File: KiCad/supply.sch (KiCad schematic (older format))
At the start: 59 parts, among them IC12 74HC00PW, IC13 SN74LVC1G126DCKR, IC4 TPS7A0518PDBVT, T3 BSS138APW, U1 LM62440-Q1, U2 LM62440-Q1

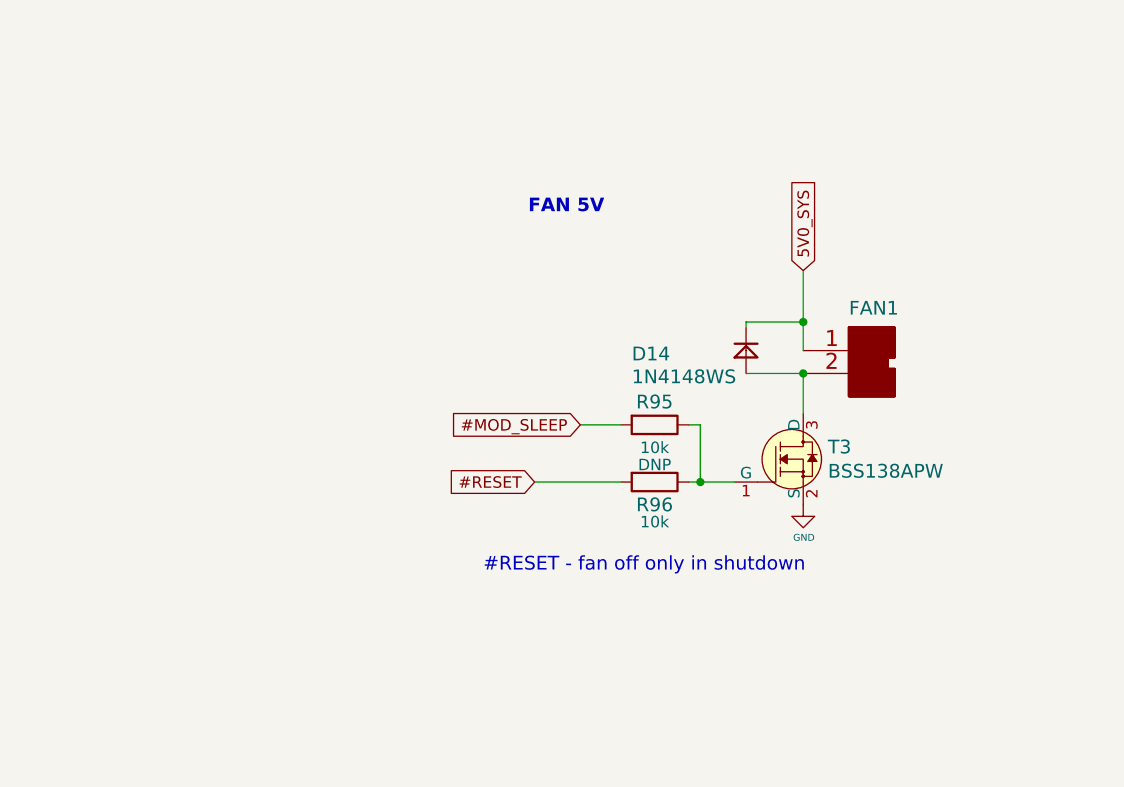
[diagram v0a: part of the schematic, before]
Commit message: Change fan design to match Nvidia. Change user button and led pins
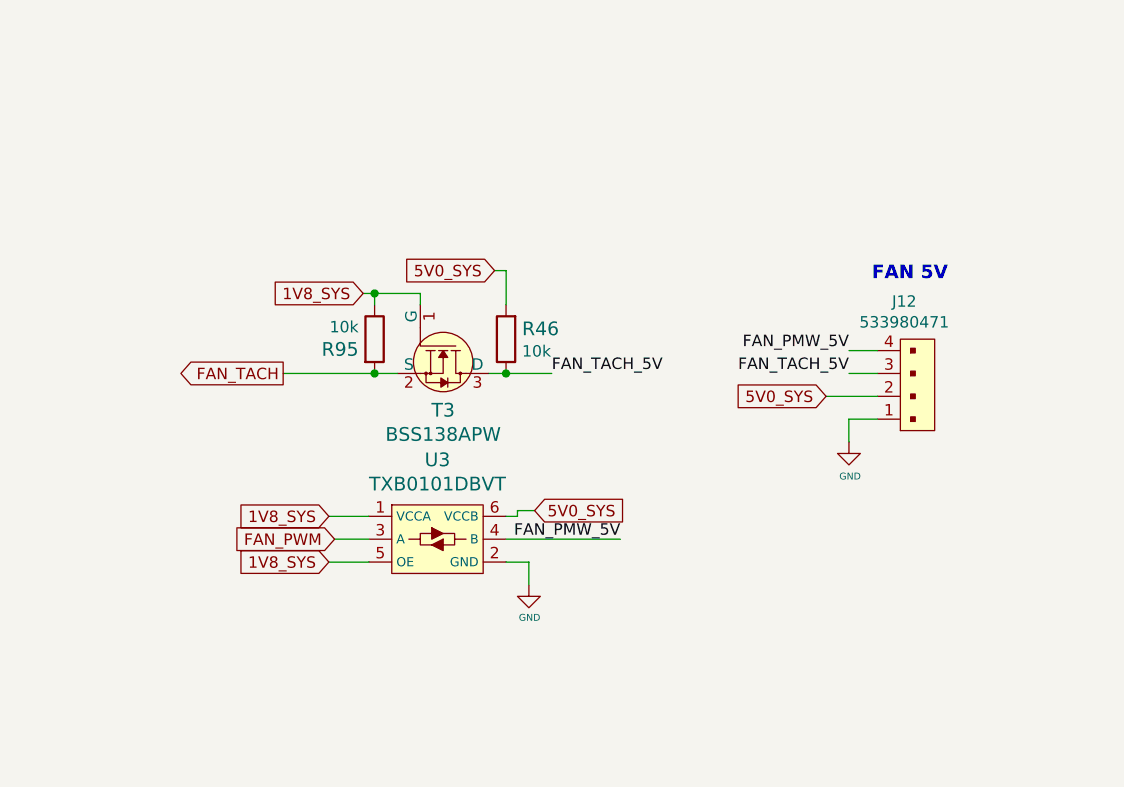
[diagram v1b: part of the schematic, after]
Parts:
- removed D14: 1N4148WS, jetson-nano-baseboard-footprints:SOD-323, symbol jetson-nano-baseboard:diode
- removed FAN1: ~, jetson-nano-baseboard-footprints:molex_2223-2021, symbol jetson-nano-baseboard:molex_2223-2021
- removed R96: R_10k_0402, jetson-nano-baseboard-footprints:0402-res, symbol jetson-nano-baseboard:R_10k_0402
- added J12: 533980471, jetson-nano-baseboard-footprints:Molex_PicoBlade_53398-0471_1x04-1MP_P1.25mm_Vertical, symbol jetson-nano-baseboard:533980471
- added R46: R_10k_0402, jetson-nano-baseboard-footprints:0402-res, symbol jetson-nano-baseboard:R_10k_0402
- added U3: TXB0101DBVT, jetson-nano-baseboard-footprints:SOT-23-6, symbol jetson-nano-baseboard:TXB0101DBVT
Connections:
- net 1V8_SYS: now also R95.1, T3.1 (G), U3.1 (VCCA), U3.5 (OE)
- net 5V0_SYS: now also J12.2, R46.2, U3.6 (VCCB)
- net GND: now also J12.1, U3.2 (GND); no longer T3.2 (S)
- net FAN_TACH_5V: now reaches T3.3 (D)
- net FAN_TACH_5V: now also J12.3, R46.1
- net #MOD_SLEEP renamed FAN_TACH
- net FAN_TACH: now also T3.2 (S)
- new net FAN_PMW_5V: J12.4, U3.4 (B)
- new net FAN_PWM: U3.3 (A)
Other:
- note removed: "#RESET - fan off only in shutdown"
- moved on the sheet: R95, T3
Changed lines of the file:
@@
 Text Notes 8075 4750 0    59   ~ 12
 Power sequencer
-Text Notes 9897 8682 0    59   ~ 12
-FAN 5V
 Wire Wire Line
 	12870 7550 12970 7550
 Wire Wire Line
 	12870 7650 12870 7550
-Text Notes 9700 10250 0    60   ~ 0
-#RESET - fan off only in shutdown
 Text Notes 9500 6575 0    60   ~ 0
 #PWR_RST
@@
 Text GLabel 13944 2408 1    50   Input ~ 0
 VIN
-Text GLabel 11100 8925 1    50   Input ~ 0
-5V0_SYS
 Text GLabel 9975 5000 1    50   Input ~ 0
 5V0_SYS
@@
 $EndComp
 $Comp
-L jetson-nano-baseboard:GND #GND_079
-U 1 1 5E7103C3
-P 11100 9950
-F 0 "#GND_079" H 11100 9950 20  0001 C CNN
-F 1 "GND" H 11103 9807 30  0000 C CNN
-F 2 "" H 11100 9950 70  0001 C CNN
-F 3 "" H 11100 9950 70  0001 C CNN
-	1    11100 9950
-	1    0    0    -1
-$EndComp
-$Comp
 L jetson-nano-baseboard:GND #GND_080
 U 1 1 5E7103C1
@@
 $EndComp
 $Comp
-L jetson-nano-baseboard:molex_2223-2021 FAN1
-U 1 1 5E7103AC
-P 11100 9275
-F 0 "FAN1" H 11300 9425 60  0000 L BNN
-F 1 "~" H 11100 9275 50  0001 C CNN
-F 2 "jetson-nano-baseboard-footprints:molex_2223-2021" H 11100 9275 50  0001 C CNN
-F 3 "" H 11100 9275 50  0001 C CNN
-F 4 "2223-2021" H 43  -12311 50  0001 C CNN "MPN"
-F 5 "Molex" H 43  -12311 50  0001 C CNN "Manufacturer"
-	1    11100 9275
-	1    0    0    -1
-$EndComp
-$Comp
-L jetson-nano-baseboard:diode D14
-U 1 1 5E7103AB
-P 10850 9275
-F 0 "D14" H 10350 9225 60  0000 L BNN
-F 1 "1N4148WS" H 10350 9125 60  0000 L BNN
-F 2 "jetson-nano-baseboard-footprints:SOD-323" H 10350 9125 60  0001 C CNN
-F 3 "" H 10350 9125 60  0001 C CNN
-F 4 "1N4148WS" H -7  -12311 50  0001 C CNN "MPN"
-F 5 "ON Semiconductor" H -7  -12311 50  0001 C CNN "Manufacturer"
-	1    10850 9275
-	1    0    0    -1
-$EndComp
-$Comp
 L jetson-nano-baseboard:Testpad TP42
 U 1 1 5E7103A8
@@
 	13875 6250 14075 6250
 Connection ~ 14075 6250
-Wire Wire Line
-	10800 9850 10650 9850
-Wire Wire Line
-	10850 9375 11100 9375
-Wire Wire Line
-	11100 9375 11100 9550
-Connection ~ 11100 9375
-Wire Wire Line
-	11100 8925 11100 9150
-Wire Wire Line
-	10850 9175 10850 9150
-Wire Wire Line
-	10850 9150 11100 9150
-Connection ~ 11100 9150
-Wire Wire Line
-	11100 9150 11100 9275
-$Comp
-L jetson-nano-baseboard:BSS138APW T3
-U 1 1 607CDC49
-P 11100 9750
-F 0 "T3" H 11208 9803 60  0000 L CNN
-F 1 "BSS138APW" H 11208 9697 60  0000 L CNN
-F 2 "jetson-nano-baseboard-footprints:SC70-3" H 11300 9950 60  0001 L CNN
-F 3 "" H 11300 10050 60  0001 L CNN
-F 4 "BSS138PW" H 11300 10250 60  0001 L CNN "MPN"
-F 5 "ON Semiconductor" H 11300 10850 60  0001 L CNN "Manufacturer"
-	1    11100 9750
-	1    0    0    -1
-$EndComp
 Text GLabel 14525 6250 2    50   Input ~ 0
 PWR_EN
-Text GLabel 9925 9850 0    50   Input ~ 0
-#RESET
 Text GLabel 9475 6450 0    50   Input ~ 0
 #SHUTDOWN_REQ
@@
 	0    1    1    0
 $EndComp
-Text GLabel 10125 9600 0    50   Input ~ 0
-#MOD_SLEEP
 Text GLabel 12225 5425 0    50   Input ~ 0
 PWR_GOOD
@@
 Wire Wire Line
 	10675 5750 10675 5000
-$Comp
-L jetson-nano-baseboard:R_10k_0402 R95
-U 1 1 6202E2C7
-P 10450 9600
-F 0 "R95" H 10450 9500 60  0000 C CNN
-F 1 "R_10k_0402" H 10450 9450 60  0001 C CNN
-F 2 "jetson-nano-baseboard-footprints:0402-res" H 10650 9800 60  0001 L CNN
-F 3 "" H 10450 9600 50  0001 C CNN
-F 4 "VISHAY" H 10650 10000 60  0001 L CNN "Manufacturer"
-F 5 "CRCW040210K0FKEDHP" H 10650 9900 60  0001 L CNN "MPN"
-F 6 "10k" H 10450 9700 50  0000 C CNN "Val"
-	1    10450 9600
-	-1   0    0    1
-$EndComp
-Wire Wire Line
-	10600 9600 10650 9600
-Wire Wire Line
-	10650 9600 10650 9850
-Wire Wire Line
-	10650 9850 10600 9850
-Connection ~ 10650 9850
-Wire Wire Line
-	9925 9850 10300 9850
-Wire Wire Line
-	10125 9600 10300 9600
 $Comp
 L jetson-nano-baseboard:R_200k_0402 R84
@@
 Wire Wire Line
 	13350 5625 13450 5625
-$Comp
-L jetson-nano-baseboard:R_10k_0402 R96
-U 1 1 6202F8EF
-P 10450 9850
-F 0 "R96" H 10450 9950 60  0000 C CNN
-F 1 "R_10k_0402" H 10450 9700 60  0001 C CNN
-F 2 "jetson-nano-baseboard-footprints:0402-res" H 10650 10050 60  0001 L CNN
-F 3 "" H 10450 9850 50  0001 C CNN
-F 4 "VISHAY" H 10650 10250 60  0001 L CNN "Manufacturer"
-F 5 "CRCW040210K0FKEDHP" H 10650 10150 60  0001 L CNN "MPN"
-F 6 "10k" H 10450 10025 50  0000 C CNN "Val"
-F 7 "DNP" H 10450 9775 50  0000 C CNN "DNP"
-	1    10450 9850
-	-1   0    0    1
-$EndComp
 $Comp
 L jetson-nano-baseboard:Testpad TP40
@@
 Wire Wire Line
 	1425 5250 2700 5250
+Text GLabel 9050 10100 0    50   Input ~ 0
+FAN_PWM
+Text GLabel 9025 10000 0    50   Input ~ 0
+1V8_SYS
+Wire Wire Line
+	9025 10000 9200 10000
+Wire Wire Line
+	9050 10100 9200 10100
+Text GLabel 9025 10200 0    50   Input ~ 0
+1V8_SYS
+Wire Wire Line
+	9025 10200 9200 10200
+Wire Wire Line
+	9800 10100 10300 10100
+Text Label 10300 10100 2    50   ~ 0
+FAN_PMW_5V
+Text GLabel 9925 9975 2    50   Input ~ 0
+5V0_SYS
+Wire Wire Line
+	9925 9975 9850 9975
+Wire Wire Line
+	9850 9975 9850 10000
+Wire Wire Line
+	9850 10000 9800 10000
+Wire Wire Line
+	9800 10200 9900 10200
+Wire Wire Line
+	9900 10200 9900 10300
+$Comp
+L jetson-nano-baseboard:GND #GND_0151
+U 1 1 61D0F309
+P 9900 10300
+F 0 "#GND_0151" H 9900 10300 20  0001 C CNN
+F 1 "GND" H 9903 10157 30  0000 C CNN
+F 2 "" H 9900 10300 70  0001 C CNN
+F 3 "" H 9900 10300 70  0001 C CNN
+	1    9900 10300
+	1    0    0    -1
+$EndComp
+$Comp
+L jetson-nano-baseboard:TXB0101DBVT U3
+U 1 1 62015C4C
+P 9500 10100
+F 0 "U3" H 9500 10447 60  0000 C CNN
+F 1 "TXB0101DBVT" H 9500 10341 60  0000 C CNN
+F 2 "jetson-nano-baseboard-footprints:SOT-23-6" H 9700 10300 60  0001 L CNN
+F 3 "https://www.ti.com/general/docs/suppproductinfo.tsp?distId=10&gotoUrl=https%3A%2F%2Fwww.ti.com%2Flit%2Fgpn%2Ftxb0101" H 9700 10400 60  0001 L CNN
+F 4 "TXB0101DBVT" H 9700 10500 60  0001 L CNN "MPN"
+F 5 "Texas Instruments" H 9700 10600 60  0001 L CNN "Manufacturer"
+	1    9500 10100
+	1    0    0    -1
+$EndComp
+Text Notes 11400 8975 0    59   ~ 12
+FAN 5V
+Text Label 11300 9375 2    50   ~ 0
+FAN_TACH_5V
+Wire Wire Line
+	11425 9375 11300 9375
+Text Label 11300 9275 2    50   ~ 0
+FAN_PMW_5V
+Wire Wire Line
+	11425 9275 11300 9275
+Text GLabel 11200 9475 0    50   Input ~ 0
+5V0_SYS
+Wire Wire Line
+	11200 9475 11425 9475
+Wire Wire Line
+	11425 9575 11300 9575
+Wire Wire Line
+	11300 9575 11300 9675
+$Comp
+L jetson-nano-baseboard:GND #GND_0157
+U 1 1 61E9E5AC
+P 11300 9675
+F 0 "#GND_0157" H 11300 9675 20  0001 C CNN
+F 1 "GND" H 11305 9525 30  0000 C CNN
+F 2 "" H 11300 9675 70  0001 C CNN
+F 3 "" H 11300 9675 70  0001 C CNN
+	1    11300 9675
+	1    0    0    -1
+$EndComp
+$Comp
+L jetson-nano-baseboard:533980471 J12
+U 1 1 6210B794
+P 11625 9425
+F 0 "J12" H 11542 9060 50  0000 C CNN
+F 1 "533980471" H 11542 9151 50  0000 C CNN
+F 2 "jetson-nano-baseboard-footprints:Molex_PicoBlade_53398-0471_1x04-1MP_P1.25mm_Vertical" H 11725 9325 50  0001 L BNN
+F 3 "https://www.molex.com/molex/products/part-detail/pcb_headers/0533980471" H 11525 9225 50  0001 L BNN
+F 4 "Molex" H 11725 9475 50  0001 L BNN "Manufacturer"
+F 5 "0533980471" H 11975 9425 50  0001 C CNN "MPN"
+	1    11625 9425
+	1    0    0    1
+$EndComp
+$Comp
+L jetson-nano-baseboard:R_10k_0402 R95
+U 1 1 6202E2C7
+P 9225 9225
+F 0 "R95" V 9270 9155 60  0000 R CNN
+F 1 "R_10k_0402" H 9225 9075 60  0001 C CNN
+F 2 "jetson-nano-baseboard-footprints:0402-res" H 9425 9425 60  0001 L CNN
+F 3 "" H 9225 9225 50  0001 C CNN
+F 4 "VISHAY" H 9425 9625 60  0001 L CNN "Manufacturer"
+F 5 "CRCW040210K0FKEDHP" H 9425 9525 60  0001 L CNN "MPN"
+F 6 "10k" V 9172 9155 50  0000 R CNN "Val"
+	1    9225 9225
+	0    1    1    0
+$EndComp
+$Comp
+L jetson-nano-baseboard:BSS138APW T3
+U 1 1 607CDC49
+P 9525 9375
+F 0 "T3" V 9686 9375 60  0000 C CNN
+F 1 "BSS138APW" V 9792 9375 60  0000 C CNN
+F 2 "jetson-nano-baseboard-footprints:SC70-3" H 9725 9575 60  0001 L CNN
+F 3 "" H 9725 9675 60  0001 L CNN
+F 4 "BSS138PW" H 9725 9875 60  0001 L CNN "MPN"
+F 5 "ON Semiconductor" H 9725 10475 60  0001 L CNN "Manufacturer"
+	1    9525 9375
+	0    1    1    0
+$EndComp
+Text GLabel 9175 9025 0    50   Input ~ 0
+1V8_SYS
+Wire Wire Line
+	9175 9025 9225 9025
+Wire Wire Line
+	9225 9075 9225 9025
+Text GLabel 8825 9375 0    50   Output ~ 0
+FAN_TACH
+$Comp
+L jetson-nano-baseboard:R_10k_0402 R46
+U 1 1 61FD0E1C
+P 9800 9225
+F 0 "R46" V 9845 9155 60  0000 R CNN
+F 1 "R_10k_0402" H 9800 9075 60  0001 C CNN
+F 2 "jetson-nano-baseboard-footprints:0402-res" H 10000 9425 60  0001 L CNN
+F 3 "" H 9800 9225 50  0001 C CNN
+F 4 "VISHAY" H 10000 9625 60  0001 L CNN "Manufacturer"
+F 5 "CRCW040210K0FKEDHP" H 10000 9525 60  0001 L CNN "MPN"
+F 6 "10k" V 9747 9155 50  0000 R CNN "Val"
+	1    9800 9225
+	0    -1   -1   0
+$EndComp
+Wire Wire Line
+	10000 9375 9800 9375
+Text GLabel 9750 8925 0    50   Input ~ 0
+5V0_SYS
+Wire Wire Line
+	9750 8925 9800 8925
+Wire Wire Line
+	9800 8925 9800 9075
+Text Label 10000 9375 0    50   ~ 0
+FAN_TACH_5V
+Connection ~ 9800 9375
+Wire Wire Line
+	9800 9375 9725 9375
+Connection ~ 9225 9375
+Wire Wire Line
+	8825 9375 9225 9375
+Wire Wire Line
+	9225 9375 9325 9375
+Wire Wire Line
+	9225 9025 9425 9025
+Wire Wire Line
+	9425 9025 9425 9075
+Connection ~ 9225 9025
 $EndSCHEMATC

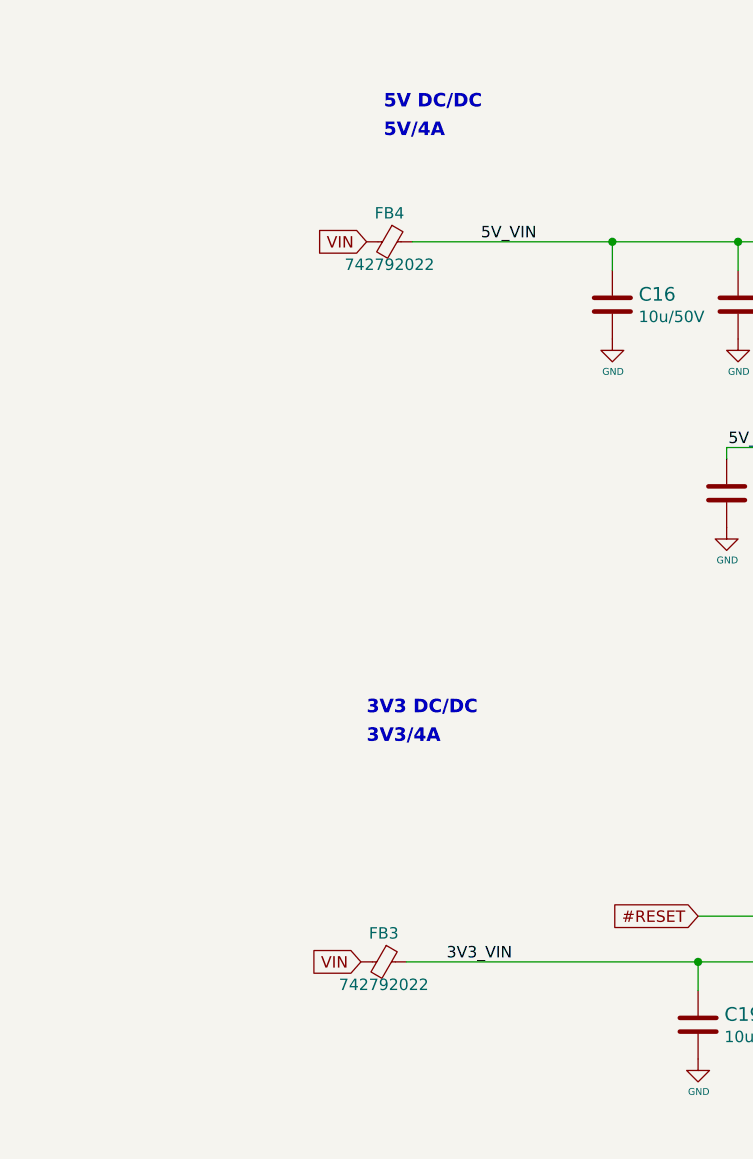
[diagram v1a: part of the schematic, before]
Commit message: 742792022  -> 74279221100
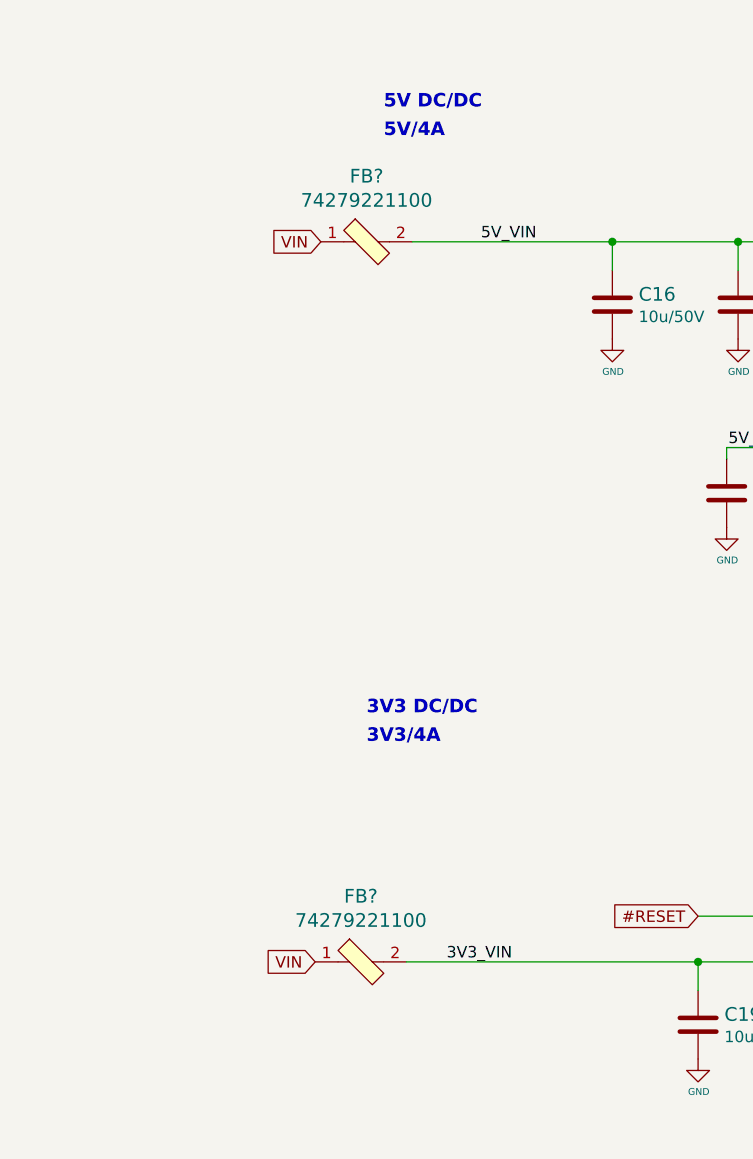
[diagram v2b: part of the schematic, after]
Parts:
- removed FB3, FB4: 742792022, jetson-nano-baseboard-footprints:0805-cap, symbol jetson-nano-baseboard:Ferrite_Bead_Small
- added FB? (x2): 74279221100, antmicro-footprints:1206-res, symbol antmicroFerriteBeadsandChips:74279221100
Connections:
- net 3V3_VIN: now also FB?.2
- net 5V_VIN: now also FB?.2
- net VIN: now also FB?.1, FB?.1
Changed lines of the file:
@@
 Text GLabel 5925 1350 0    50   Input ~ 0
 5V0_SYS
-$Comp
-L jetson-nano-baseboard:Ferrite_Bead_Small FB4
-U 1 1 61C66316
-P 1350 2100
-F 0 "FB4" V 1225 2100 50  0000 C CNN
-F 1 "742792022 " V 1450 2100 50  0000 C CNN
-F 2 "jetson-nano-baseboard-footprints:0805-cap" V 1280 2100 50  0001 C CNN
-F 3 "~" H 1350 2100 50  0001 C CNN
-	1    1350 2100
-	0    1    1    0
-$EndComp
-Text GLabel 1250 2100 0    50   Input ~ 0
+Text GLabel 1050 2100 0    50   Input ~ 0
 VIN
 Wire Wire Line
@@
 Text Label 3325 5050 0    50   ~ 0
 3V3_EN
-$Comp
-L jetson-nano-baseboard:Ferrite_Bead_Small FB3
-U 1 1 61E2F9C4
-P 1325 5250
-F 0 "FB3" V 1200 5250 50  0000 C CNN
-F 1 "742792022 " V 1425 5250 50  0000 C CNN
-F 2 "jetson-nano-baseboard-footprints:0805-cap" V 1255 5250 50  0001 C CNN
-F 3 "~" H 1325 5250 50  0001 C CNN
-	1    1325 5250
-	0    1    1    0
-$EndComp
-Text GLabel 1225 5250 0    50   Input ~ 0
+Text GLabel 1025 5250 0    50   Input ~ 0
 VIN
 $Comp
@@
 	9425 9025 9425 9075
 Connection ~ 9225 9025
+$Comp
+L antmicroFerriteBeadsandChips:74279221100 FB?
+U 1 1 624FA3DC
+P 1250 2100
+F 0 "FB?" H 1250 2387 60  0000 C CNN
+F 1 "74279221100" H 1250 2281 60  0000 C CNN
+F 2 "antmicro-footprints:1206-res" H 1450 2300 60  0001 L CNN
+F 3 "https://www.we-online.com/catalog/datasheet/74279221100.pdf" H 1450 2400 60  0001 L CNN
+F 4 "74279221100" H 1450 2600 60  0001 L CNN "MPN"
+F 5 "Wurth Electronic" H 1450 3200 60  0001 L CNN "Manufacturer"
+	1    1250 2100
+	1    0    0    -1
+$EndComp
+$Comp
+L antmicroFerriteBeadsandChips:74279221100 FB?
+U 1 1 6250F269
+P 1225 5250
+F 0 "FB?" H 1225 5537 60  0000 C CNN
+F 1 "74279221100" H 1225 5431 60  0000 C CNN
+F 2 "antmicro-footprints:1206-res" H 1425 5450 60  0001 L CNN
+F 3 "https://www.we-online.com/catalog/datasheet/74279221100.pdf" H 1425 5550 60  0001 L CNN
+F 4 "74279221100" H 1425 5750 60  0001 L CNN "MPN"
+F 5 "Wurth Electronic" H 1425 6350 60  0001 L CNN "Manufacturer"
+	1    1225 5250
+	1    0    0    -1
+$EndComp
 $EndSCHEMATC
